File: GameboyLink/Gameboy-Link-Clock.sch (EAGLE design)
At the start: 37 parts, among them IC1 MEGA8-AI, J1 AVR_SPI_PRG_6PTH, Q1 16MHz, U1 DS1307Z, Y1 32.768kHz

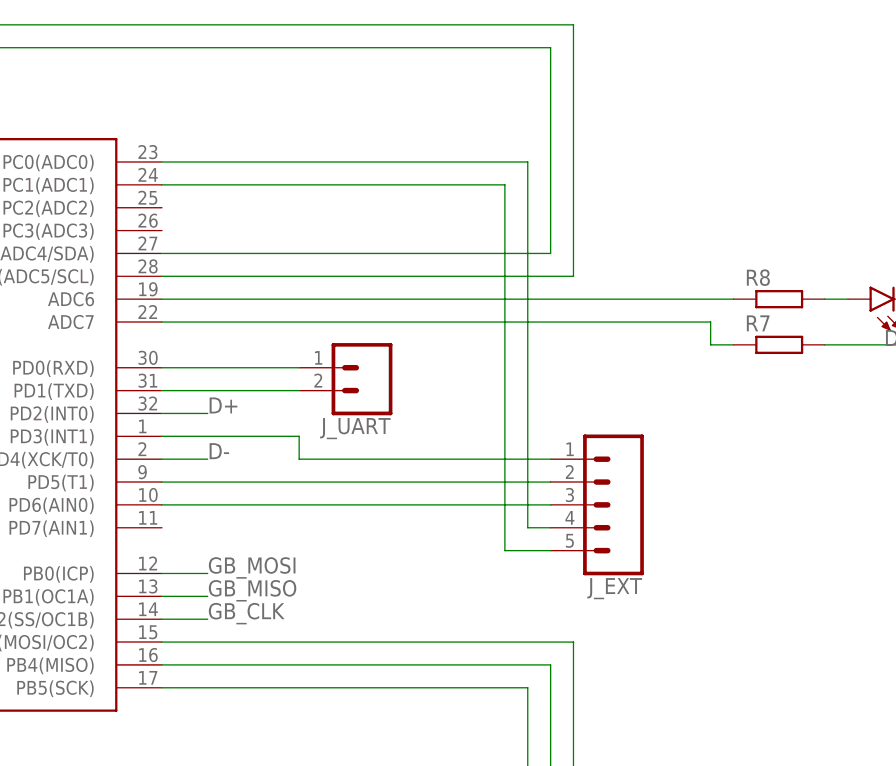
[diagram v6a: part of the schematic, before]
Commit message: Routing done draft!  Need to add ADC channels
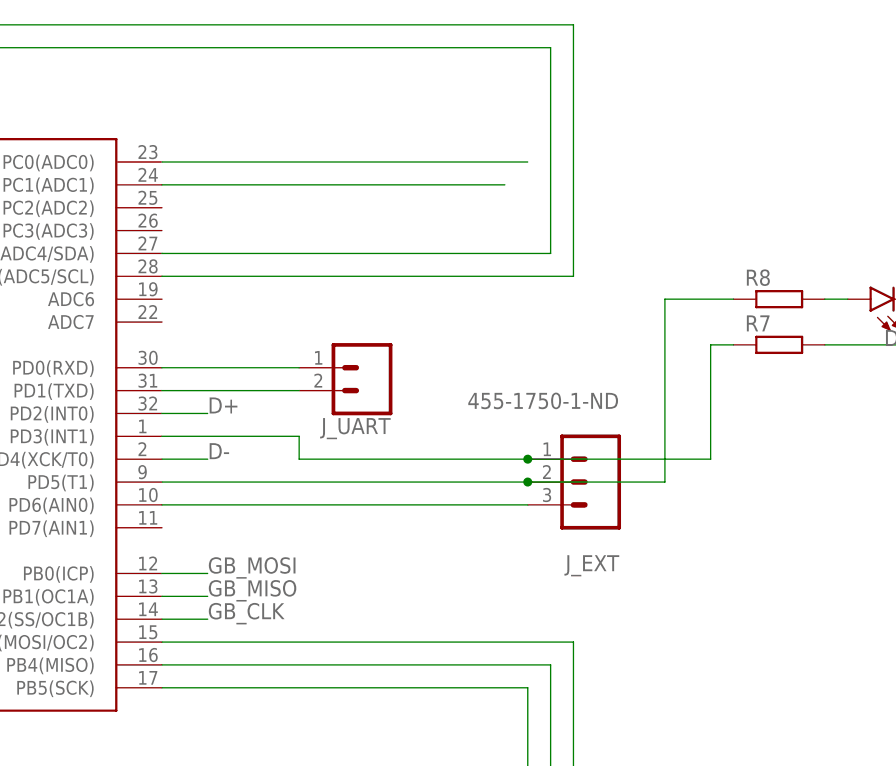
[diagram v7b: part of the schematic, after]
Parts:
- J_EXT: value (none) -> 455-1750-1-ND; device SparkFun-Connectors:CONN_05PTH -> SparkFun-Connectors:CONN_03
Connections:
- removed net N$10: IC1.PD5(T1), J_EXT.2
- removed net N$21: IC1.ADC6, R8.1
- removed net N$22: IC1.ADC7, R7.1
- removed net N$6: IC1.PD3(INT1), J_EXT.1
- new net N$17: IC1.PD5(T1), J_EXT.2, R8.1
- new net N$9: IC1.PD3(INT1), J_EXT.1, R7.1
- net N$15: no longer J_EXT.5
- net N$18: no longer J_EXT.4
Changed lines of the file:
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@@
 <setting verticaltext="up"/>
 </settings>
-<grid distance="0.1" unitdist="inch" unit="inch" style="lines" multiple="1" display="yes" altdistance="0.01" altunitdist="inch" altunit="inch"/>
+<grid distance="0.1" unitdist="inch" unit="inch" style="lines" multiple="1" display="no" altdistance="0.01" altunitdist="inch" altunit="inch"/>
 <layers>
 <layer number="1" name="Top" color="4" fill="1" visible="no" active="no"/>
@@
 <part name="C6" library="rcl" library_urn="urn:adsk.eagle:library:334" deviceset="CPOL-EU" device="150CLZ-1014" package3d_urn="urn:adsk.eagle:package:23405/2"/>
 <part name="J_POWER" library="SparkFun-Connectors" deviceset="CONN_02" device=""/>
-<part name="J_EXT" library="SparkFun-Connectors" deviceset="CONN_05" device="PTH"/>
+<part name="J_EXT" library="SparkFun-Connectors" deviceset="CONN_03" device="" value="455-1750-1-ND"/>
 <part name="R7" library="rcl" library_urn="urn:adsk.eagle:library:334" deviceset="R-EU_" device="R1206" package3d_urn="urn:adsk.eagle:package:23540/2"/>
 <part name="R8" library="rcl" library_urn="urn:adsk.eagle:library:334" deviceset="R-EU_" device="R1206" package3d_urn="urn:adsk.eagle:package:23540/2"/>
@@
 <attribute name="NAME" x="86.36" y="-164.592" size="1.778" layer="95" font="vector"/>
 </instance>
-<instance part="J_EXT" gate="J1" x="251.46" y="-139.7" smashed="yes" rot="R180">
-<attribute name="VALUE" x="254" y="-129.794" size="1.778" layer="96" font="vector" rot="R180"/>
-<attribute name="NAME" x="254" y="-147.828" size="1.778" layer="95" font="vector" rot="R180"/>
+<instance part="J_EXT" gate="J1" x="248.92" y="-137.16" smashed="yes" rot="R180">
+<attribute name="VALUE" x="251.46" y="-127.254" size="1.778" layer="96" font="vector" rot="R180"/>
+<attribute name="NAME" x="251.46" y="-145.288" size="1.778" layer="95" font="vector" rot="R180"/>
 </instance>
 <instance part="R7" gate="G$1" x="269.24" y="-121.92" smashed="yes">
@@
 </segment>
 </net>
-<net name="N$10" class="0">
-<segment>
+<net name="N$11" class="0">
+<segment>
+<pinref part="IC1" gate="G$1" pin="PD6(AIN0)"/>
+<pinref part="J_EXT" gate="J1" pin="3"/>
+<wire x1="200.66" y1="-139.7" x2="241.3" y2="-139.7" width="0.1524" layer="91"/>
+</segment>
+</net>
+<net name="N$18" class="0">
+<segment>
+<pinref part="IC1" gate="G$1" pin="PC0(ADC0)"/>
+<wire x1="241.3" y1="-101.6" x2="200.66" y2="-101.6" width="0.1524" layer="91"/>
+</segment>
+</net>
+<net name="N$15" class="0">
+<segment>
+<pinref part="IC1" gate="G$1" pin="PC1(ADC1)"/>
+<wire x1="200.66" y1="-104.14" x2="238.76" y2="-104.14" width="0.1524" layer="91"/>
+</segment>
+</net>
+<net name="N$19" class="0">
+<segment>
+<pinref part="R8" gate="G$1" pin="2"/>
+<pinref part="D2" gate="D1" pin="A"/>
+<wire x1="274.32" y1="-116.84" x2="276.86" y2="-116.84" width="0.1524" layer="91"/>
+</segment>
+</net>
+<net name="N$20" class="0">
+<segment>
+<pinref part="R7" gate="G$1" pin="2"/>
+<pinref part="D3" gate="D1" pin="A"/>
+<wire x1="274.32" y1="-121.92" x2="284.48" y2="-121.92" width="0.1524" layer="91"/>
+</segment>
+</net>
+<net name="N$23" class="0">
+<segment>
+<pinref part="U1" gate="G$1" pin="X1"/>
+<wire x1="149.86" y1="-55.88" x2="149.86" y2="-60.96" width="0.1524" layer="91"/>
+<pinref part="Y1" gate="G$1" pin="1"/>
+<wire x1="142.24" y1="-55.88" x2="149.86" y2="-55.88" width="0.1524" layer="91"/>
+</segment>
+</net>
+<net name="N$24" class="0">
+<segment>
+<pinref part="U1" gate="G$1" pin="X2"/>
+<wire x1="137.16" y1="-63.5" x2="149.86" y2="-63.5" width="0.1524" layer="91"/>
+<pinref part="Y1" gate="G$1" pin="2"/>
+<wire x1="137.16" y1="-55.88" x2="137.16" y2="-63.5" width="0.1524" layer="91"/>
+</segment>
+</net>
+<net name="N$17" class="0">
+<segment>
+<pinref part="R8" gate="G$1" pin="1"/>
+<wire x1="264.16" y1="-116.84" x2="256.54" y2="-116.84" width="0.1524" layer="91"/>
+<wire x1="256.54" y1="-116.84" x2="256.54" y2="-137.16" width="0.1524" layer="91"/>
 <pinref part="IC1" gate="G$1" pin="PD5(T1)"/>
 <pinref part="J_EXT" gate="J1" pin="2"/>
-<wire x1="200.66" y1="-137.16" x2="243.84" y2="-137.16" width="0.1524" layer="91"/>
-</segment>
-</net>
-<net name="N$11" class="0">
-<segment>
-<pinref part="IC1" gate="G$1" pin="PD6(AIN0)"/>
-<pinref part="J_EXT" gate="J1" pin="3"/>
-<wire x1="200.66" y1="-139.7" x2="243.84" y2="-139.7" width="0.1524" layer="91"/>
-</segment>
-</net>
-<net name="N$6" class="0">
-<segment>
+<wire x1="200.66" y1="-137.16" x2="241.3" y2="-137.16" width="0.1524" layer="91"/>
+<wire x1="256.54" y1="-137.16" x2="241.3" y2="-137.16" width="0.1524" layer="91"/>
+<junction x="241.3" y="-137.16"/>
+</segment>
+</net>
+<net name="N$9" class="0">
+<segment>
+<pinref part="R7" gate="G$1" pin="1"/>
+<wire x1="264.16" y1="-121.92" x2="261.62" y2="-121.92" width="0.1524" layer="91"/>
+<wire x1="261.62" y1="-121.92" x2="261.62" y2="-134.62" width="0.1524" layer="91"/>
 <pinref part="IC1" gate="G$1" pin="PD3(INT1)"/>
 <wire x1="200.66" y1="-132.08" x2="215.9" y2="-132.08" width="0.1524" layer="91"/>
 <wire x1="215.9" y1="-132.08" x2="215.9" y2="-134.62" width="0.1524" layer="91"/>
 <pinref part="J_EXT" gate="J1" pin="1"/>
-<wire x1="215.9" y1="-134.62" x2="243.84" y2="-134.62" width="0.1524" layer="91"/>
-</segment>
-</net>
-<net name="N$18" class="0">
-<segment>
-<pinref part="IC1" gate="G$1" pin="PC0(ADC0)"/>
-<wire x1="241.3" y1="-101.6" x2="200.66" y2="-101.6" width="0.1524" layer="91"/>
-<pinref part="J_EXT" gate="J1" pin="4"/>
-<wire x1="241.3" y1="-101.6" x2="241.3" y2="-142.24" width="0.1524" layer="91"/>
-<wire x1="241.3" y1="-142.24" x2="243.84" y2="-142.24" width="0.1524" layer="91"/>
-</segment>
-</net>
-<net name="N$15" class="0">
-<segment>
-<pinref part="IC1" gate="G$1" pin="PC1(ADC1)"/>
-<wire x1="200.66" y1="-104.14" x2="238.76" y2="-104.14" width="0.1524" layer="91"/>
-<wire x1="238.76" y1="-104.14" x2="238.76" y2="-144.78" width="0.1524" layer="91"/>
-<pinref part="J_EXT" gate="J1" pin="5"/>
-<wire x1="238.76" y1="-144.78" x2="243.84" y2="-144.78" width="0.1524" layer="91"/>
-</segment>
-</net>
-<net name="N$19" class="0">
-<segment>
-<pinref part="R8" gate="G$1" pin="2"/>
-<pinref part="D2" gate="D1" pin="A"/>
-<wire x1="274.32" y1="-116.84" x2="276.86" y2="-116.84" width="0.1524" layer="91"/>
-</segment>
-</net>
-<net name="N$20" class="0">
-<segment>
-<pinref part="R7" gate="G$1" pin="2"/>
-<pinref part="D3" gate="D1" pin="A"/>
-<wire x1="274.32" y1="-121.92" x2="284.48" y2="-121.92" width="0.1524" layer="91"/>
-</segment>
-</net>
-<net name="N$21" class="0">
-<segment>
-<pinref part="R8" gate="G$1" pin="1"/>
-<pinref part="IC1" gate="G$1" pin="ADC6"/>
-<wire x1="264.16" y1="-116.84" x2="200.66" y2="-116.84" width="0.1524" layer="91"/>
-</segment>
-</net>
-<net name="N$22" class="0">
-<segment>
-<pinref part="R7" gate="G$1" pin="1"/>
-<wire x1="261.62" y1="-121.92" x2="264.16" y2="-121.92" width="0.1524" layer="91"/>
-<wire x1="261.62" y1="-121.92" x2="261.62" y2="-119.38" width="0.1524" layer="91"/>
-<pinref part="IC1" gate="G$1" pin="ADC7"/>
-<wire x1="261.62" y1="-119.38" x2="200.66" y2="-119.38" width="0.1524" layer="91"/>
-</segment>
-</net>
-<net name="N$23" class="0">
-<segment>
-<pinref part="U1" gate="G$1" pin="X1"/>
-<wire x1="149.86" y1="-55.88" x2="149.86" y2="-60.96" width="0.1524" layer="91"/>
-<pinref part="Y1" gate="G$1" pin="1"/>
-<wire x1="142.24" y1="-55.88" x2="149.86" y2="-55.88" width="0.1524" layer="91"/>
-</segment>
-</net>
-<net name="N$24" class="0">
-<segment>
-<pinref part="U1" gate="G$1" pin="X2"/>
-<wire x1="137.16" y1="-63.5" x2="149.86" y2="-63.5" width="0.1524" layer="91"/>
-<pinref part="Y1" gate="G$1" pin="2"/>
-<wire x1="137.16" y1="-55.88" x2="137.16" y2="-63.5" width="0.1524" layer="91"/>
-</segment>
-</net>
+<wire x1="215.9" y1="-134.62" x2="241.3" y2="-134.62" width="0.1524" layer="91"/>
+<wire x1="261.62" y1="-134.62" x2="241.3" y2="-134.62" width="0.1524" layer="91"/>
+<junction x="241.3" y="-134.62"/>
+</segment>
+</net>

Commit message: All routed, now cosmetics and indepth review.
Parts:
- added J_ADC: (no value), SparkFun-Connectors:CONN_02
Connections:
- net GND: now also IC1.GND@2
- net N$15: now also J_ADC.2
- net N$18: now also J_ADC.1
- net VCC: now also IC1.VCC@2
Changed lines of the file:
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@@
 <part name="R2" library="rcl" library_urn="urn:adsk.eagle:library:334" deviceset="R-EU_" device="R1206" package3d_urn="urn:adsk.eagle:package:23540/2" value="10k"/>
 <part name="J_GB_DBG" library="SparkFun-Connectors" deviceset="CONN_03X2" device="FEMALE" value="FEMALE 2x3"/>
+<part name="J_ADC" library="SparkFun-Connectors" deviceset="CONN_02" device=""/>
 </parts>
 <sheets>
@@
 </instance>
 <instance part="J_EXT" gate="J1" x="248.92" y="-137.16" smashed="yes" rot="R180">
-<attribute name="VALUE" x="251.46" y="-127.254" size="1.778" layer="96" font="vector" rot="R180"/>
 <attribute name="NAME" x="251.46" y="-145.288" size="1.778" layer="95" font="vector" rot="R180"/>
 </instance>
@@
 <attribute name="NAME" x="75.184" y="-57.912" size="1.778" layer="95" font="vector"/>
 <attribute name="VALUE" x="75.438" y="-69.342" size="1.778" layer="96" font="vector" align="top-left"/>
+</instance>
+<instance part="J_ADC" gate="J1" x="231.14" y="-101.6" smashed="yes" rot="R180">
+<attribute name="VALUE" x="233.68" y="-96.774" size="1.778" layer="96" font="vector" rot="R180"/>
+<attribute name="NAME" x="233.68" y="-107.188" size="1.778" layer="95" font="vector" rot="R180"/>
 </instance>
 </instances>
@@
 <wire x1="127" y1="-119.38" x2="119.38" y2="-119.38" width="0.1524" layer="91"/>
 <junction x="119.38" y="-119.38"/>
+<pinref part="IC1" gate="G$1" pin="GND@2"/>
+<wire x1="152.4" y1="-134.62" x2="152.4" y2="-132.08" width="0.1524" layer="91"/>
+<junction x="152.4" y="-132.08"/>
 </segment>
 <segment>
@@
 <wire x1="152.4" y1="-111.76" x2="124.46" y2="-111.76" width="0.1524" layer="91"/>
 <junction x="124.46" y="-111.76"/>
+<pinref part="IC1" gate="G$1" pin="VCC@2"/>
+<wire x1="152.4" y1="-139.7" x2="152.4" y2="-137.16" width="0.1524" layer="91"/>
+<junction x="152.4" y="-137.16"/>
 </segment>
 <segment>
@@
 <segment>
 <pinref part="IC1" gate="G$1" pin="PC0(ADC0)"/>
-<wire x1="241.3" y1="-101.6" x2="200.66" y2="-101.6" width="0.1524" layer="91"/>
+<pinref part="J_ADC" gate="J1" pin="1"/>
+<wire x1="223.52" y1="-101.6" x2="200.66" y2="-101.6" width="0.1524" layer="91"/>
 </segment>
 </net>
@@
 <segment>
 <pinref part="IC1" gate="G$1" pin="PC1(ADC1)"/>
-<wire x1="200.66" y1="-104.14" x2="238.76" y2="-104.14" width="0.1524" layer="91"/>
-</segment>
-</net>
+<wire x1="200.66" y1="-104.14" x2="223.52" y2="-104.14" width="0.1524" layer="91"/>
+<pinref part="J_ADC" gate="J1" pin="2"/>
+</segment>
+</net>
